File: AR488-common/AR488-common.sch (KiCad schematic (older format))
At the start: 9 parts, among them J1 Conn_02x12_Top_Bottom, J2 Conn_02x12_Odd_Even, J3 Barrel_Jack, J4 Screw_Terminal_01x02, U2 SN75162BDW, U3 SN75160BDW

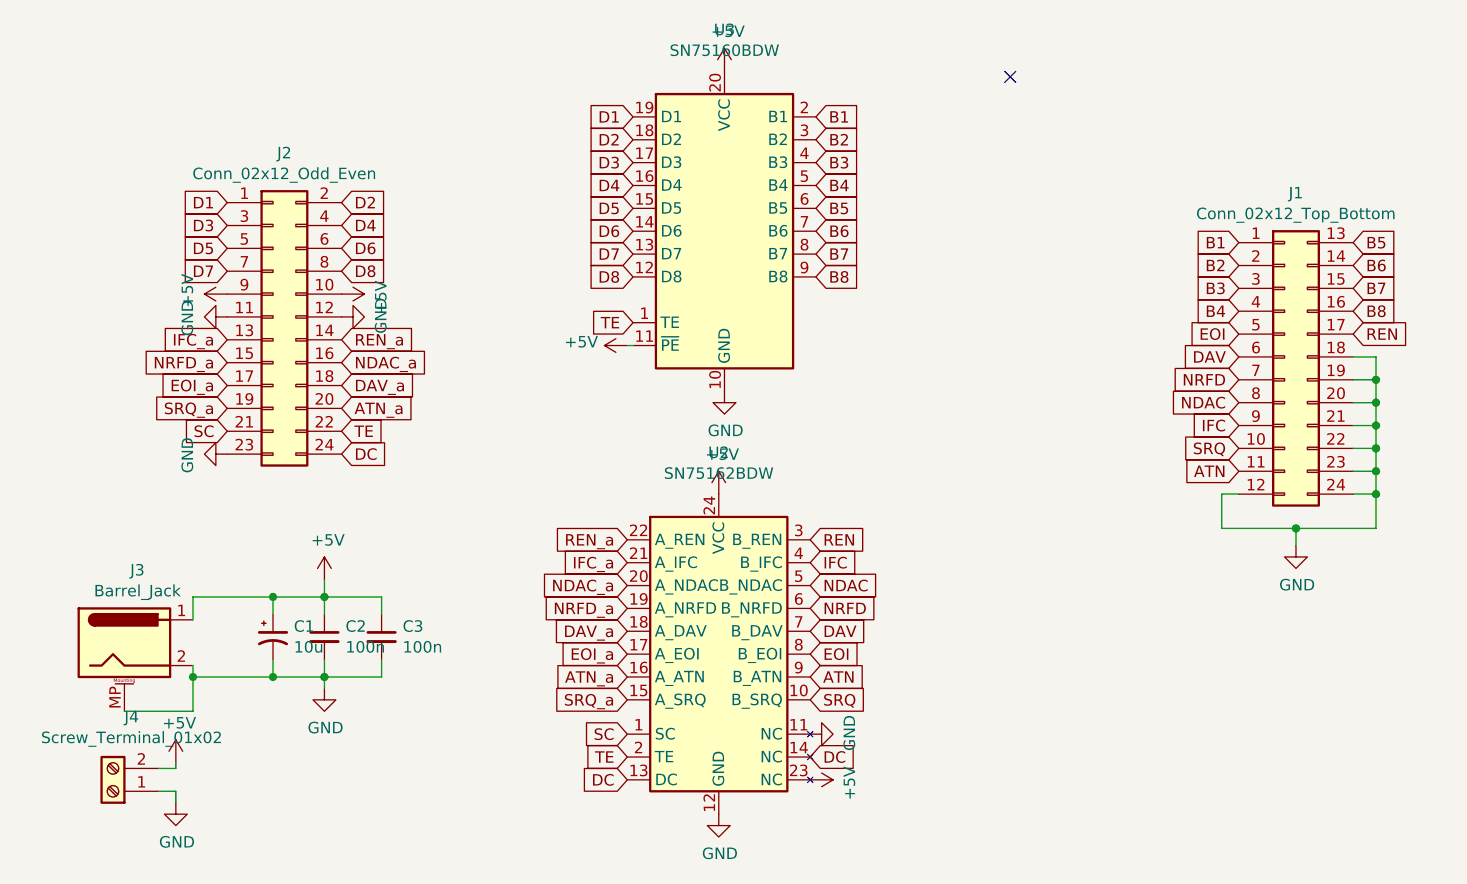
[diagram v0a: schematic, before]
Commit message: Finish the commons board + esp32 s2 soala + esp32 devkitc boards
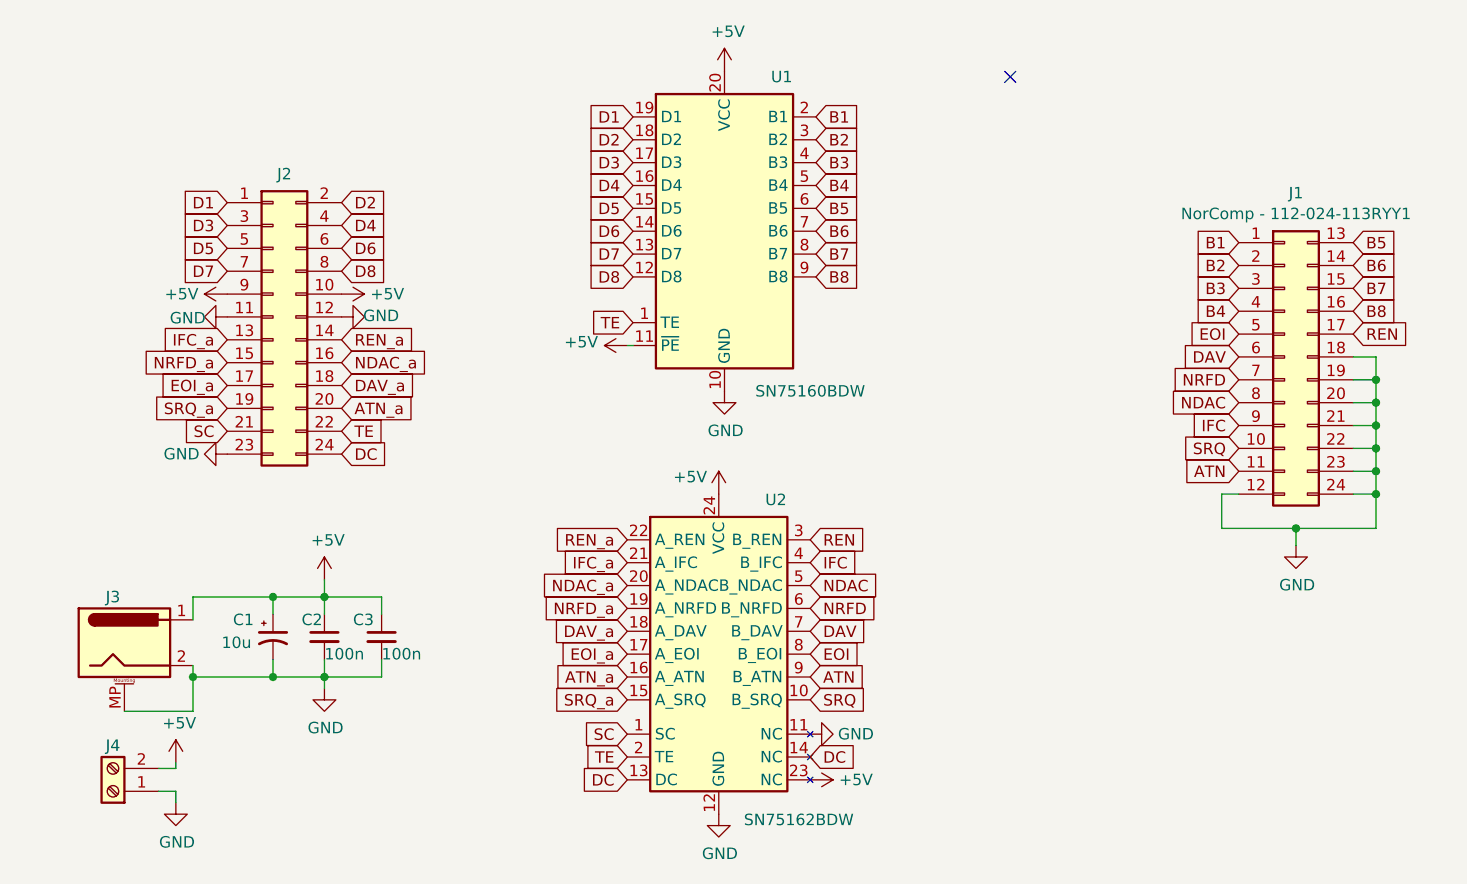
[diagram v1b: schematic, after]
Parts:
- J1: value Conn_02x12_Top_Bottom -> NorComp - 112-024-113RYY1
- renumbered U3 to U1
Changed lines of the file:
@@
 $EndDescr
 $Comp
-L Interface:SN75160BDW U3
+L Interface:SN75160BDW U1
 U 1 1 6167419F
 P 5650 1800
-F 0 "U3" H 5650 2681 50  0000 C CNN
-F 1 "SN75160BDW" H 5650 2590 50  0000 C CNN
+F 0 "U1" H 5900 2475 50  0000 C CNN
+F 1 "SN75160BDW" H 6025 1100 50  0000 C CNN
 F 2 "Package_SO:SOIC-20W_7.5x12.8mm_P1.27mm" H 5650 1500 50  0001 C CNN
 F 3 "http://www.ti.com/lit/ds/symlink/sn75160b.pdf" H 5600 2150 50  0001 C CNN
@@
 P 8100 2350
 F 0 "J1" H 8150 3067 50  0000 C CNN
-F 1 "Conn_02x12_Top_Bottom" H 8150 2976 50  0000 C CNN
+F 1 "NorComp - 112-024-113RYY1" H 8150 2976 50  0000 C CNN
 F 2 "misc:CENTRONICS-24" H 8100 2350 50  0001 C CNN
 F 3 "~" H 8100 2350 50  0001 C CNN
@@
 P 5625 2950
 F 0 "#PWR04" H 5625 2800 50  0001 C CNN
-F 1 "+5V" H 5640 3123 50  0000 C CNN
+F 1 "+5V" H 5500 3025 50  0000 C CNN
 F 2 "" H 5625 2950 50  0001 C CNN
 F 3 "" H 5625 2950 50  0001 C CNN
@@
 U 1 1 617ED5E6
 P 3675 2175
-F 0 "J2" H 3725 2892 50  0000 C CNN
-F 1 "Conn_02x12_Odd_Even" H 3725 2801 50  0000 C CNN
+F 0 "J2" H 3725 2800 50  0000 C CNN
+F 1 "Conn_02x12_Odd_Even" H 3725 2801 50  0001 C CNN
 F 2 "Connector_PinSocket_2.54mm:PinSocket_2x12_P2.54mm_Vertical" H 3675 2175 50  0001 C CNN
 F 3 "~" H 3675 2175 50  0001 C CNN
@@
 P 3975 2175
 F 0 "#PWR010" H 3975 1925 50  0001 C CNN
-F 1 "GND" H 3980 2002 50  0000 C CNN
+F 1 "GND" V 3980 2002 50  0000 C CNN
 F 2 "" H 3975 2175 50  0001 C CNN
 F 3 "" H 3975 2175 50  0001 C CNN
@@
 P 3475 2175
 F 0 "#PWR03" H 3475 1925 50  0001 C CNN
-F 1 "GND" H 3480 2002 50  0000 C CNN
+F 1 "GND" V 3480 2002 50  0000 C CNN
 F 2 "" H 3475 2175 50  0001 C CNN
 F 3 "" H 3475 2175 50  0001 C CNN
@@
 P 3975 2075
 F 0 "#PWR09" H 3975 1925 50  0001 C CNN
-F 1 "+5V" H 3990 2248 50  0000 C CNN
+F 1 "+5V" V 3975 2275 50  0000 C CNN
 F 2 "" H 3975 2075 50  0001 C CNN
 F 3 "" H 3975 2075 50  0001 C CNN
@@
 P 3475 2075
 F 0 "#PWR02" H 3475 1925 50  0001 C CNN
-F 1 "+5V" H 3490 2248 50  0000 C CNN
+F 1 "+5V" V 3475 2275 50  0000 C CNN
 F 2 "" H 3475 2075 50  0001 C CNN
 F 3 "" H 3475 2075 50  0001 C CNN
@@
 P 3475 2775
 F 0 "#PWR01" H 3475 2525 50  0001 C CNN
-F 1 "GND" H 3480 2602 50  0000 C CNN
+F 1 "GND" V 3475 2575 50  0000 C CNN
 F 2 "" H 3475 2775 50  0001 C CNN
 F 3 "" H 3475 2775 50  0001 C CNN
@@
 U 1 1 6180EAFE
 P 3675 3575
-F 0 "C1" H 3766 3621 50  0000 L CNN
-F 1 "10u" H 3766 3530 50  0000 L CNN
+F 0 "C1" H 3500 3650 50  0000 L CNN
+F 1 "10u" H 3450 3550 50  0000 L CNN
 F 2 "Capacitor_Tantalum_SMD:CP_EIA-7132-20_AVX-U" H 3675 3575 50  0001 C CNN
 F 3 "~" H 3675 3575 50  0001 C CNN
@@
 U 1 1 618102D7
 P 3900 3575
-F 0 "C2" H 3992 3621 50  0000 L CNN
-F 1 "100n" H 3992 3530 50  0000 L CNN
+F 0 "C2" H 3800 3650 50  0000 L CNN
+F 1 "100n" H 3900 3500 50  0000 L CNN
 F 2 "Capacitor_SMD:C_1206_3216Metric" H 3900 3575 50  0001 C CNN
 F 3 "~" H 3900 3575 50  0001 C CNN
@@
 U 1 1 618111BF
 P 4150 3575
-F 0 "C3" H 4242 3621 50  0000 L CNN
-F 1 "100n" H 4242 3530 50  0000 L CNN
+F 0 "C3" H 4025 3650 50  0000 L CNN
+F 1 "100n" H 4150 3500 50  0000 L CNN
 F 2 "Capacitor_SMD:C_1206_3216Metric" H 4150 3575 50  0001 C CNN
 F 3 "~" H 4150 3575 50  0001 C CNN
@@
 U 1 1 6182B7AF
 P 3025 3600
-F 0 "J3" H 3082 3917 50  0000 C CNN
-F 1 "Barrel_Jack" H 3082 3826 50  0000 C CNN
+F 0 "J3" H 2975 3800 50  0000 C CNN
+F 1 "Barrel_Jack" H 3082 3826 50  0001 C CNN
 F 2 "Connector_BarrelJack:BarrelJack_CUI_PJ-063AH_Horizontal" H 3075 3560 50  0001 C CNN
 F 3 "~" H 3075 3560 50  0001 C CNN
@@
 U 1 1 618381F0
 P 2975 4250
-F 0 "J4" H 2893 3925 50  0000 C CNN
-F 1 "Screw_Terminal_01x02" H 2893 4016 50  0000 C CNN
+F 0 "J4" H 2975 4050 50  0000 C CNN
+F 1 "Screw_Terminal_01x02" H 2250 4175 50  0001 C CNN
 F 2 "TerminalBlock:TerminalBlock_Altech_AK300-2_P5.00mm" H 2975 4250 50  0001 C CNN
 F 3 "~" H 2975 4250 50  0001 C CNN
@@
 U 1 1 6167818E
 P 5625 3650
-F 0 "U2" H 5625 4531 50  0000 C CNN
-F 1 "SN75162BDW" H 5625 4440 50  0000 C CNN
+F 0 "U2" H 5875 4325 50  0000 C CNN
+F 1 "SN75162BDW" H 5975 2925 50  0000 C CNN
 F 2 "Package_SO:SOIC-24W_7.5x15.4mm_P1.27mm" H 5625 3370 50  0001 C CNN
 F 3 "http://www.ti.com/lit/ds/symlink/sn75162b.pdf" H 5575 4000 50  0001 C CNN
@@
 P 6025 4000
 F 0 "#PWR0106" H 6025 3750 50  0001 C CNN
-F 1 "GND" H 6030 3827 50  0000 C CNN
+F 1 "GND" V 6025 3800 50  0000 C CNN
 F 2 "" H 6025 4000 50  0001 C CNN
 F 3 "" H 6025 4000 50  0001 C CNN
@@
 P 6025 4200
 F 0 "#PWR0107" H 6025 4050 50  0001 C CNN
-F 1 "+5V" H 6040 4373 50  0000 C CNN
+F 1 "+5V" V 6025 4400 50  0000 C CNN
 F 2 "" H 6025 4200 50  0001 C CNN
 F 3 "" H 6025 4200 50  0001 C CNN
